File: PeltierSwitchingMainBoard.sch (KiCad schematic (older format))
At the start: 52 parts, among them J1 +12VIn, J10 Conn_01x02, J11 Conn_01x02, J2 GNDIn, J3 Molex Micro Lock (1.25mm 1.5A), J4 Conn_01x02, J5 Conn_01x02, J6 Conn_01x02, J7 Conn_01x02, J8 Conn_01x02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

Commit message: Almost finalized designing single board
Signed-off-by: bebenlebricolo <benoittarrade@hotmail.fr>
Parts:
- added H1, H2, H3, H4: MountingHole_Pad, MountingHole:MountingHole_4mm_Pad_TopOnly, symbol Mechanical:MountingHole_Pad
- added R12, R18, R19: 0, Resistor_SMD:R_2512_6332Metric_Pad1.40x3.35mm_HandSolder, symbol Device:R
- added R13, R14, R15, R16, R17, R20: 0, Resistor_SMD:R_1206_3216Metric_Pad1.30x1.75mm_HandSolder, symbol Device:R
- U2, U3, U4, U5: footprint STD80N6F6:STD80N6F6 -> Package_TO_SOT_SMD:TO-252-2
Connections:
- net +12V: now also R15.2, R19.1, R19.2; no longer D1.2 (A), D2.2 (A), U1.15 (VCC), U1.16 (VDD)
- net AHO: now also R13.2; no longer R7.2, TP4.1
- net ALO: now also R16.2; no longer R8.2, TP3.1
- net ALS: now also R14.2; no longer C10.1, C11.1, C9.1, J3.5 (Pin_5), R9.1, TP7.1, U1.17 (BLS), U3.3 (S), U5.3 (S)
- net Disable: now also J3.2 (Pin_2); no longer J3.3 (Pin_3)
- net GND: now also J3.3 (Pin_3), H1.1, H2.1, H3.1, H4.1, R18.1, R18.2, R20.1; no longer U1.4 (VSS)
- net HEN: now also J3.1 (Pin_1); no longer J3.4 (Pin_4)
- net IN+: now also J3.4 (Pin_4); no longer J3.1 (Pin_1)
- net IN-: now also J3.5 (Pin_5); no longer J3.2 (Pin_2)
- net VSense: now reaches J3.6 (Pin_6)
- net VSense: now also C10.1, C11.1, R9.1, TP7.1, U5.3 (S), R12.1, R17.2
- new net: D1.2 (A), D2.2 (A), R15.1, U1.15 (VCC), U1.16 (VDD)
- new net: R20.2, U1.4 (VSS)
- new net: C9.1, R12.2, R14.1, U3.3 (S)
- new net AHO-gate: R13.1, R7.2, TP4.1
- new net ALO-gate: R16.1, R8.2, TP3.1
- new net BLS: R17.1, U1.17 (BLS)
- no-connect marks 1 -> 0
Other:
- note added: "Jumpers (because no vias)"

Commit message: Added mezzanine footprint
Signed-off-by: bebenlebricolo <benoittarrade@hotmail.fr>
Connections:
- net PeltierRight is gone; now on net BHS: J10.2 (Pin_2), J11.2 (Pin_2), J4.2 (Pin_2), J5.2 (Pin_2), J6.2 (Pin_2), J7.2 (Pin_2), J8.2 (Pin_2), J9.2 (Pin_2), U4.3 (S), U5.2 (D)
- net AHS: now reaches C8.2, U1.12 (AHS)
- net AHS: now also L1.1, L2.1, L3.1, L4.1, U2.3 (S), U3.2 (D)
- net BHS: now reaches C7.2, U1.19 (BHS)
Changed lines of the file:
@@
 $EndComp
 Wire Wire Line
-	7700 2800 7700 3200
+	7700 2800 7700 2950
 Wire Wire Line
 	7700 1650 7700 2300
@@
 	1    0    0    -1
 $EndComp
-Wire Wire Line
-	6200 2800 6200 3250
 Wire Wire Line
 	6200 2300 6200 1650
@@
 	-1   0    0    1
 $EndComp
+Wire Wire Line
+	6200 2800 6200 2950
+Wire Wire Line
+	6200 2950 5900 2950
+Connection ~ 6200 2950
+Wire Wire Line
+	6200 2950 6200 3250
+Text Label 5900 2950 2    50   ~ 0
+AHS
+Wire Wire Line
+	7700 2950 8000 2950
+Connection ~ 7700 2950
+Wire Wire Line
+	7700 2950 7700 3200
+Text Label 8000 2950 0    50   ~ 0
+BHS
+Wire Wire Line
+	4150 3550 4450 3550
+Connection ~ 4150 3550
+Text Label 4450 3550 0    50   ~ 0
+BHS
+Wire Wire Line
+	4300 4150 4450 4150
+Connection ~ 4300 4150
+Text Label 4450 4150 0    50   ~ 0
+AHS
 $EndSCHEMATC

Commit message: Modified silkscreen and added cooling fans connectors
Signed-off-by: bebenlebricolo <benoittarrade@hotmail.fr>
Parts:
- removed C6: 100nF, Capacitor_SMD:C_1206_3216Metric_Pad1.33x1.80mm_HandSolder, symbol Device:C
- removed C7, C8: 330nF, Capacitor_SMD:C_1206_3216Metric_Pad1.33x1.80mm_HandSolder, symbol Device:C
- removed D1, D2: 1N4148W, Diode_SMD:D_SOD-123, symbol Diode:1N4148W
- removed J3: Molex Micro Lock (1.25mm 1.5A), PeltierSwitchingMainBoard:Molex_MicroLock_1.25_01x06, symbol Connector_Generic:Conn_01x06
- removed R12, R18, R19: 0, Resistor_SMD:R_2512_6332Metric_Pad1.40x3.35mm_HandSolder, symbol Device:R
- removed R13, R14, R15, R16, R17, R20: 0, Resistor_SMD:R_1206_3216Metric_Pad1.30x1.75mm_HandSolder, symbol Device:R
- removed R3, R5, R6: 10k, Resistor_SMD:R_1206_3216Metric_Pad1.30x1.75mm_HandSolder, symbol Device:R
- removed R4: 56k, Resistor_SMD:R_1206_3216Metric_Pad1.30x1.75mm_HandSolder, symbol Device:R
- removed TP1, TP2, TP3, TP4, TP5, TP6, TP7, TP8: TestPoint, TestPoint:TestPoint_Pad_D2.0mm, symbol Connector:TestPoint
- removed U1: HIP4080A, Package_SO:SOIC-20W_7.5x12.8mm_P1.27mm, symbol Driver_FET:HIP4080A
- added J12, J13, J14, J15, J16, J17, J18, J19: Conn_01x02, Connector_PinHeader_2.54mm:PinHeader_1x02_P2.54mm_Vertical_SMD_Pin1Left, symbol Connector_Generic:Conn_01x02
- added J3: Conn_01x14, Connector_PinHeader_2.54mm:PinHeader_1x14_P2.54mm_Vertical_SMD_Pin1Left, symbol Connector_Generic:Conn_01x14
- R1, R2: value 10k -> 0; footprint Resistor_SMD:R_1206_3216Metric_Pad1.30x1.75mm_HandSolder -> Resistor_SMD:R_2512_6332Metric_Pad1.40x3.35mm_HandSolder
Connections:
- net AHO-gate is gone; now on net AHO: R7.2
- net ALO-gate is gone; now on net ALO: R8.2
- net IN+ is gone; now on net +12V: R1.1
- net IN- is gone; now on net GND: R2.1
- net VSense is gone; now on net ALS: C10.1, C11.1, R9.1, U5.3 (S)
- net +12V: now also R1.2, J12.1 (Pin_1), J13.1 (Pin_1), J14.1 (Pin_1), J15.1 (Pin_1), J16.1 (Pin_1), J17.1 (Pin_1), J18.1 (Pin_1), J19.1 (Pin_1), J3.11 (Pin_11), J3.13 (Pin_13)
- net AHO: now also J3.3 (Pin_3)
- net AHS: now also J3.2 (Pin_2)
- net ALO: now also J3.4 (Pin_4)
- net ALS: now also C9.1, U3.3 (S), J3.12 (Pin_12), J3.5 (Pin_5), J3.9 (Pin_9)
- net BHO: now also J3.7 (Pin_7)
- net BHS: now also J3.10 (Pin_10)
- net BLO: now also J3.8 (Pin_8)
- net GND: now also J12.2 (Pin_2), J13.2 (Pin_2), J14.2 (Pin_2), J15.2 (Pin_2), J16.2 (Pin_2), J17.2 (Pin_2), J18.2 (Pin_2), J19.2 (Pin_2), J3.14 (Pin_14); no longer R1.2
- no-connect marks 0 -> 2
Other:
- note added: "Peltier fans connectors (40x40mm fans)\n- No throttling"
- note removed: "Jumpers (because no vias)"
- moved on the sheet: J1, J2

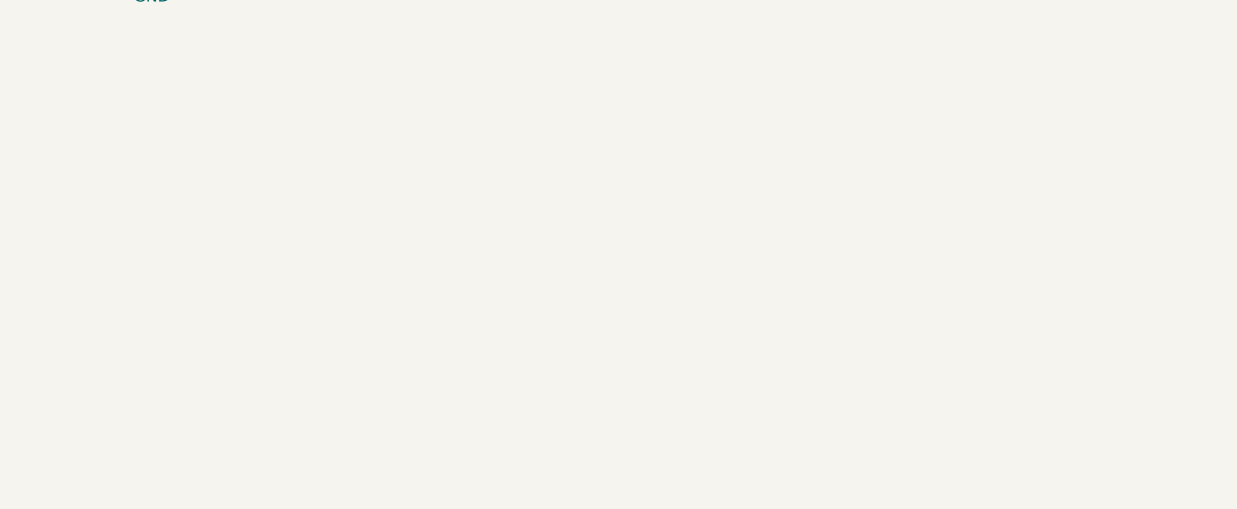
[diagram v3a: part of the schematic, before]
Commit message: Updated schematic and silkscreen
Signed-off-by: bebenlebricolo <benoittarrade@hotmail.fr>
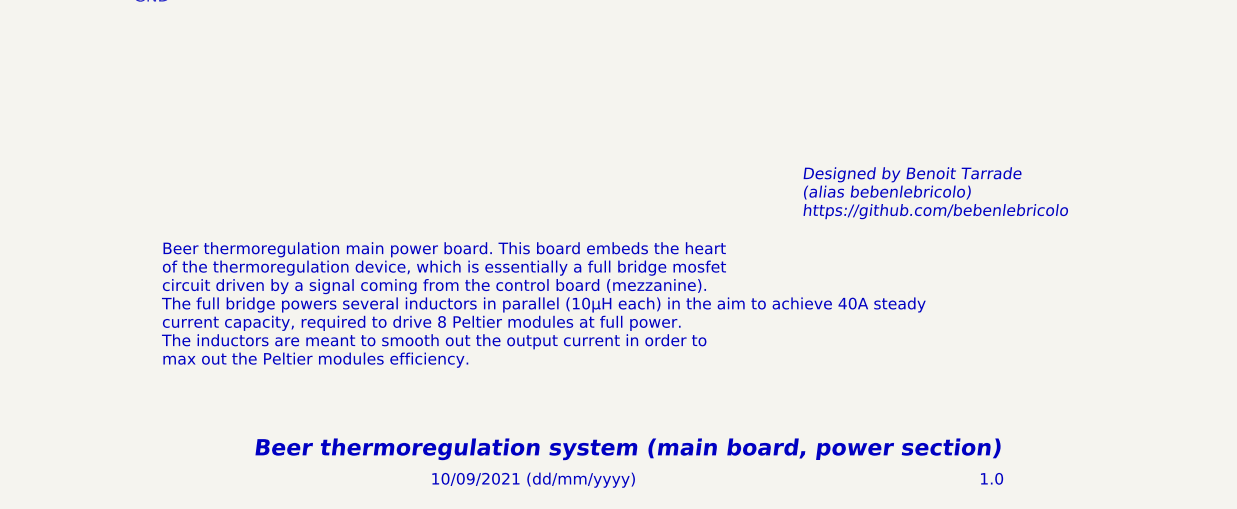
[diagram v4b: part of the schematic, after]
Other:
- note added: "1.0"
- note added: "10/09/2021 (dd/mm/yyyy)"
- note added: "Beer thermoregulation main power board. This board embeds the heart\nof the thermoregulation device, which is essentially a full bridge mosfet\ncircuit driven by a signal coming from the control board (mezzanine).\nThe full bridge powers several inductors in parallel (10µH each) in the aim to achieve 40A steady \ncurrent capacity, required to drive 8 Peltier modules at full power.\nThe inductors 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"
- note added: "Beer thermoregulation system (main board, power section)"
- note added: "Designed by Benoit Tarrade\n(alias bebenlebricolo)\nhttps://github.com/bebenlebricolo"
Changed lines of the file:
@@
 Text Notes 1900 4700 0    50   ~ 0
 Peltier fans connectors (40x40mm fans)\n- No throttling
+Text Notes 7400 7500 0    71   Italic 14
+Beer thermoregulation system (main board, power section)
+Text Notes 10575 7625 0    50   ~ 0
+1.0
+Text Notes 8175 7625 0    50   ~ 0
+10/09/2021 (dd/mm/yyyy)
+Text Notes 7000 7100 0    50   ~ 0
+Beer thermoregulation main power board. This board embeds the heart\nof the thermoregulation device, which is essentially a full bridge mosfet\ncircuit driven by a signal coming from the control board (mezzanine).\nThe full bridge powers several inductors in parallel (10µH each) in the aim to achieve 40A steady \ncurrent capacity, required to drive 8 Peltier modules at full power.\nThe inductors are meant to smooth out the output current in order to\nmax out the Peltier modules efficiency.
+Text Notes 9800 6450 0    50   Italic 0
+Designed by Benoit Tarrade\n(alias bebenlebricolo)\nhttps://github.com/bebenlebricolo
 $EndSCHEMATC
